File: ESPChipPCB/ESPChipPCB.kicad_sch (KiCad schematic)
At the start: 30 parts, among them J1 Conn_01x02, J2 Conn_01x02, J3 Conn_01x02, J4 USB_OTG, Q1 BPW40, Q2 BPW40, U1 ESP32-C3-WROOM-02

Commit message: More pcb stuff
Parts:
- removed J4: USB_OTG, symbol Connector:USB_OTG
- added J4, J6: Conn_01x02, Connector_PinHeader_2.54mm:PinHeader_1x02_P2.54mm_Vertical, symbol Connector_Generic:Conn_01x02
- added J5: Conn_01x04, symbol Connector_Generic:Conn_01x04
- added R10: R, Resistor_SMD:R_0603_1608Metric, symbol Device:R
- added SW1: SW_Push, symbol Switch:SW_Push
- D2, D3: footprint LED_SMD:LED-APA102-2020 -> LED_THT:LED_D5.0mm_Clear
- R8, R9: value 10K -> 10k
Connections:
- net +3.3V: now also R8.2, R9.2, J5.4 (Pin_4), J6.2 (Pin_2), R10.2; no longer R8.1, R9.1
- net D+: now also J4.2 (Pin_2)
- net D-: now also J4.1 (Pin_1)
- net FirstSensor: now also U1.15 (IO3)
- net GND: now also D3.1 (K), J5.1 (Pin_1), J6.1 (Pin_1), SW1.1
- net SecondSensor: now also U1.4 (IO5)
- net at U1.16 (IO2): now also R9.1; no longer R8.2
- net at U1.7 (IO8): now also R8.1; no longer R9.2
- net at U1.8 (IO9): now also SW1.2
- net at D2.2 (A): now also R10.1; no longer D3.1 (K)
- new net RX: J5.3 (Pin_3)
- new net TX: J5.2 (Pin_2)
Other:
- moved on the sheet: D2, D3, J1, J3, R5

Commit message: Moved from arduino to platformio , redone some of the code
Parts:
- removed C1, C2: 10u/1206, Capacitor_SMD:C_0603_1608Metric, symbol Device:C
- removed C3: 22n, Capacitor_SMD:C_0603_1608Metric, symbol Device:C
- removed C4, C5: 22u, Capacitor_SMD:C_0603_1608Metric, symbol Device:C
- removed C6: 100p, Capacitor_SMD:C_0603_1608Metric, symbol Device:C
- removed D1: B340A, Diode_SMD:D_SMA, symbol Device:D_Schottky
- removed J5: Conn_01x04, symbol Connector_Generic:Conn_01x04
- removed L1: 10u/C2921170, Inductor_SMD:L_Chilisin_BMRA00040420, symbol Device:L
- removed PS1: AP5100WG-7, SamacSys:SOT95P285X140-6N, symbol SamacSys_Parts:AP5100WG-7
- removed R3: 10k, Resistor_SMD:R_0603_1608Metric, symbol Device:R
- removed R4: 3.3k, Resistor_SMD:R_0603_1608Metric, symbol Device:R
- added U2: ~, SamacSys:StepDown3v3, symbol SamacSys:StepDown3v3
- R1: MPN C25804 -> (none)
- R2: value 2k -> 10k; MPN C22975 -> (none)
- S1: value EN -> Trigger; footprint SamacSys:463092691402 -> SamacSys:SwitchSmall
- SW1: footprint (none) -> Jumper:SolderJumper-2_P1.3mm_Open_RoundedPad1.0x1.5mm
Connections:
- net +3.3V: now also U2.3 (3v3)
- net +BATT: now also R1.1, U2.2 (BATT); no longer R1.2
- net GND: now also R2.2, U2.1 (GND); no longer R2.1
- net at S1.1 (COM): now also R1.2, R2.1
- new net: S1.2 (NO), U2.4 (EN)

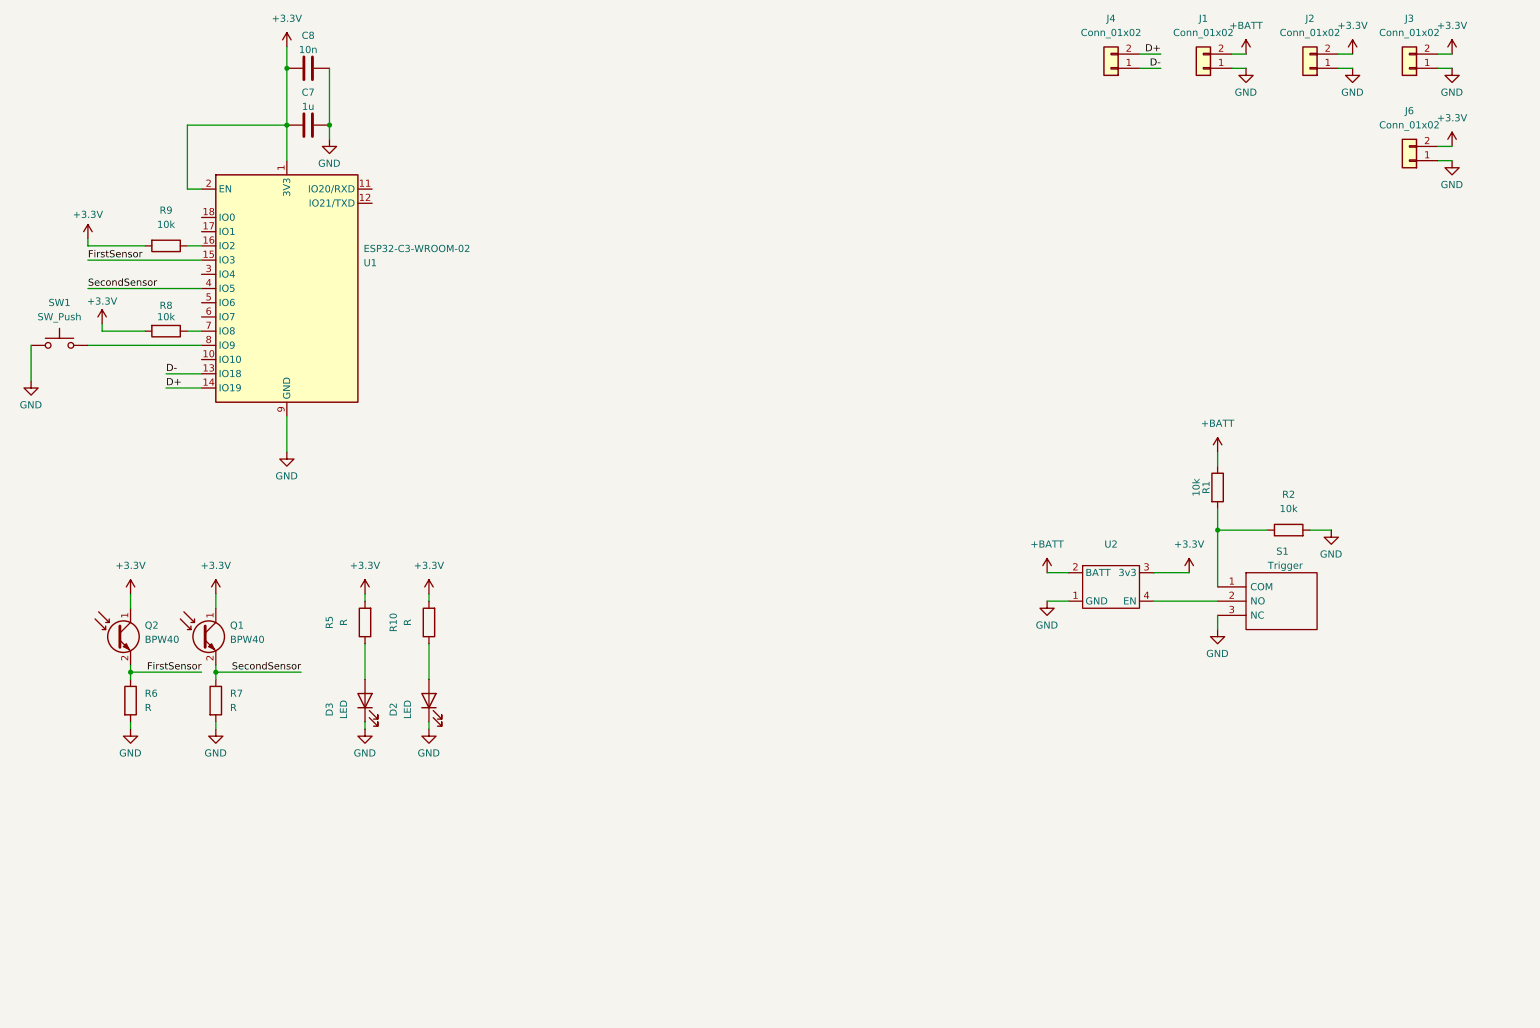
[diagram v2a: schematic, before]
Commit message: Redone logic and calculations
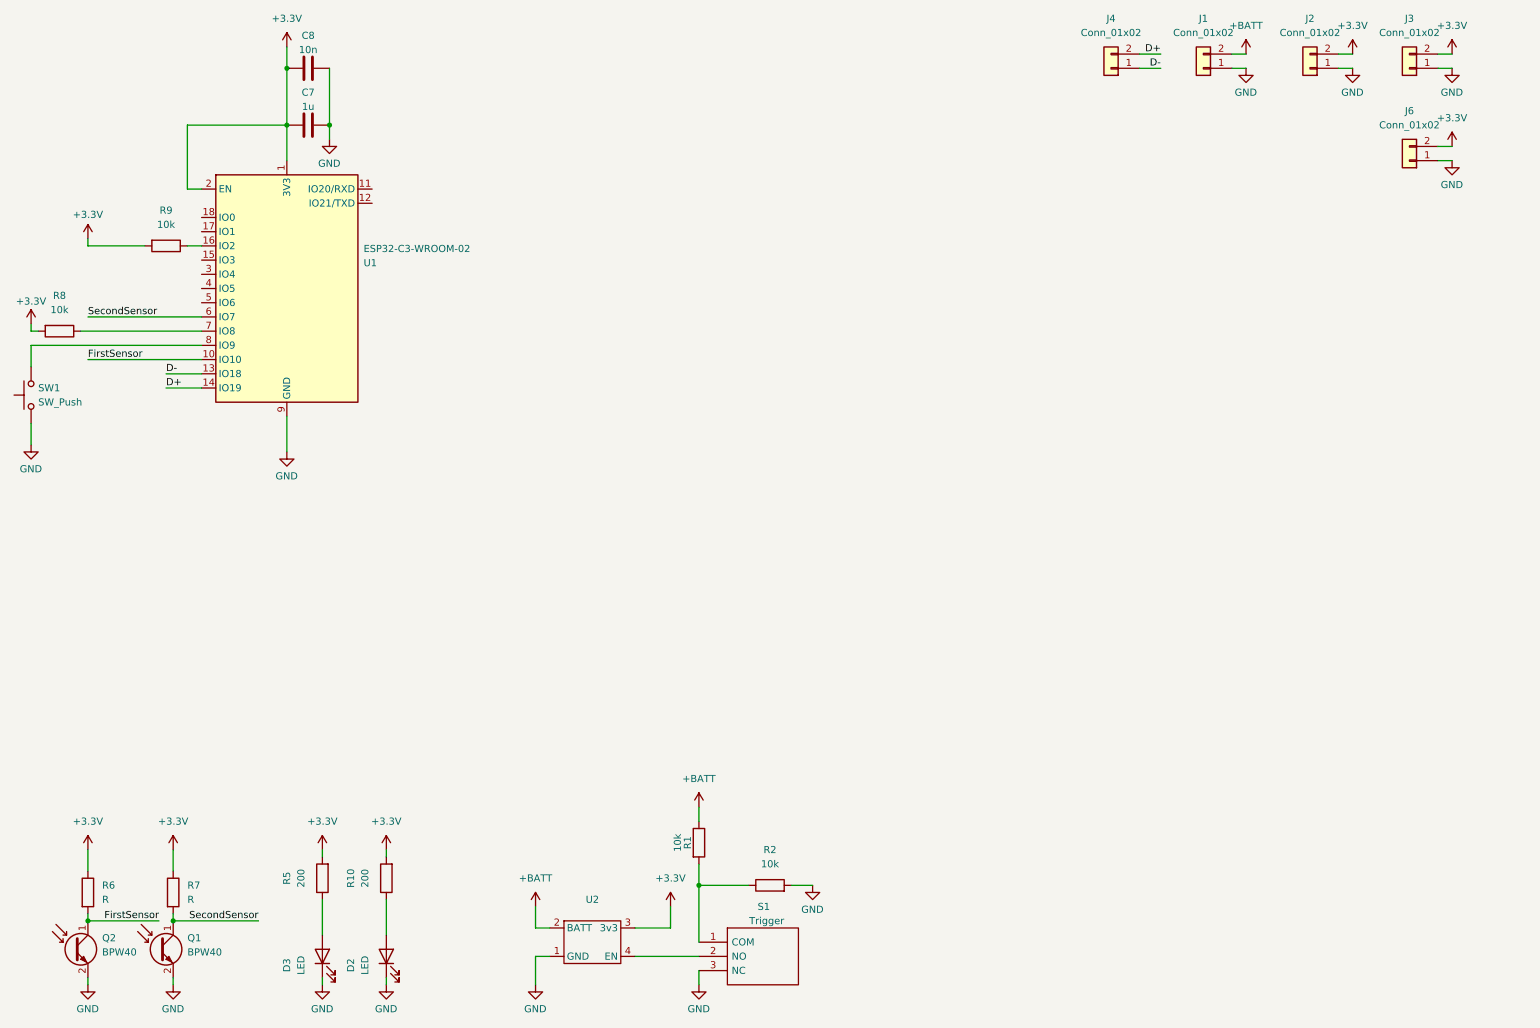
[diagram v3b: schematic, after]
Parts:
- R10, R5: value R -> 200
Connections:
- net +3.3V: now also R6.1, R7.1; no longer Q1.1 (C), Q2.1 (C)
- net FirstSensor: now also Q2.1 (C), R6.2, U1.10 (IO10); no longer Q2.2 (E), R6.1, U1.15 (IO3)
- net GND: now also Q1.2 (E), Q2.2 (E); no longer R6.2, R7.2
- net SecondSensor: now also Q1.1 (C), R7.2, U1.6 (IO7); no longer Q1.2 (E), R7.1, U1.4 (IO5)
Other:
- moved on the sheet: D2, D3, Q1, Q2, R1, R10, R2, R5, R6, R7, R8, S1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
